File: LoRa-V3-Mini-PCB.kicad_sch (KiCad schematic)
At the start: 23 parts, among them Q1 NA, SW1 Application Button, SW2 MCU Reset, U1 Lora-E5, U2 BR24G1MFVT, U3 SHT40, U4 TSL25911

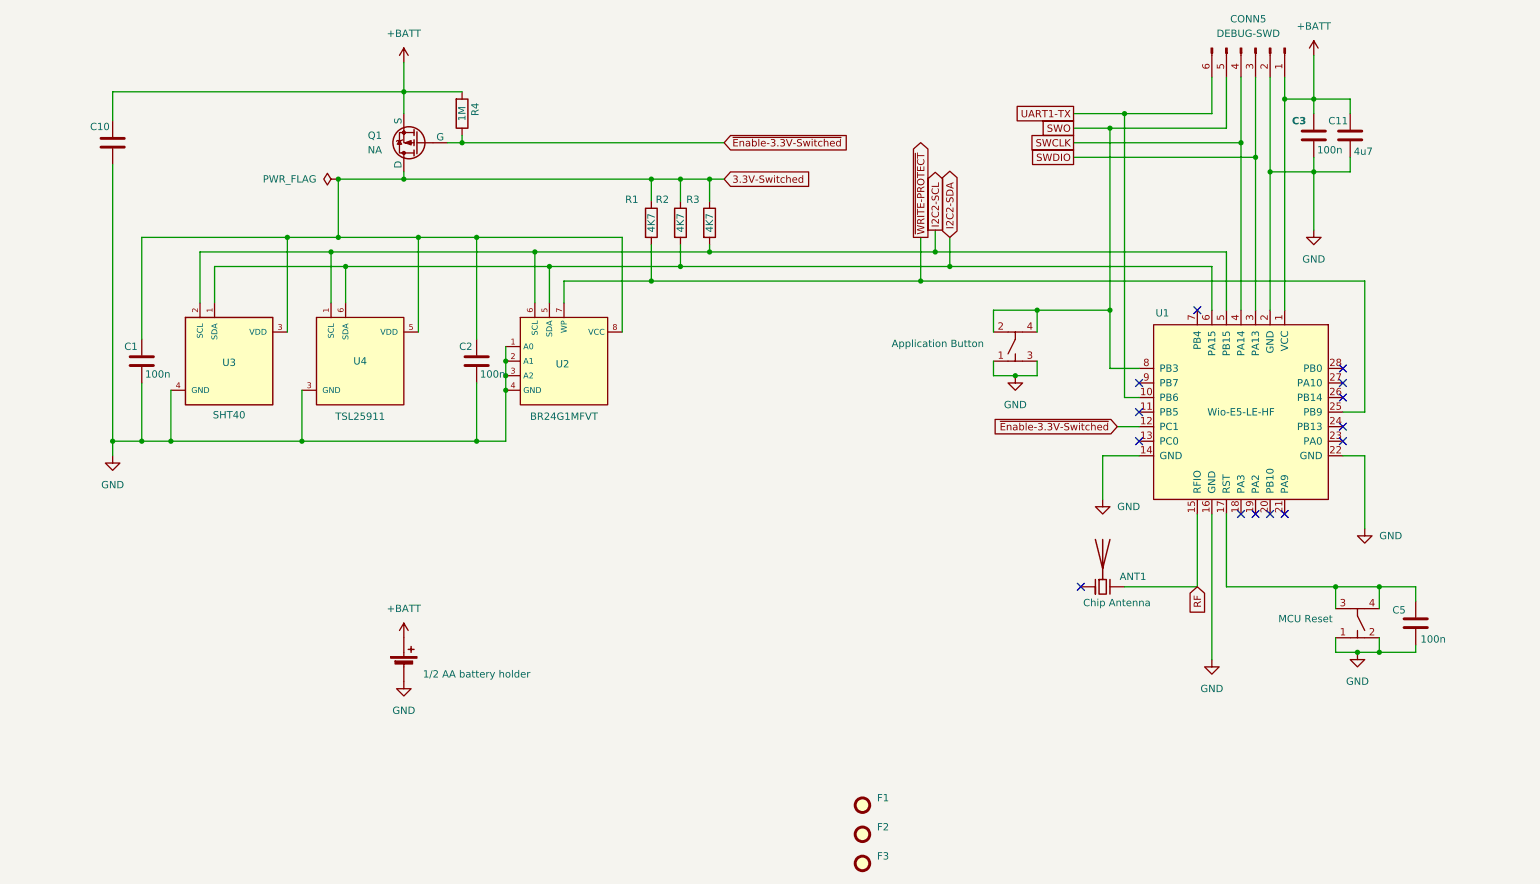
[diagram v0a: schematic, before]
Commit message: try fix error on GND needing datasheet...
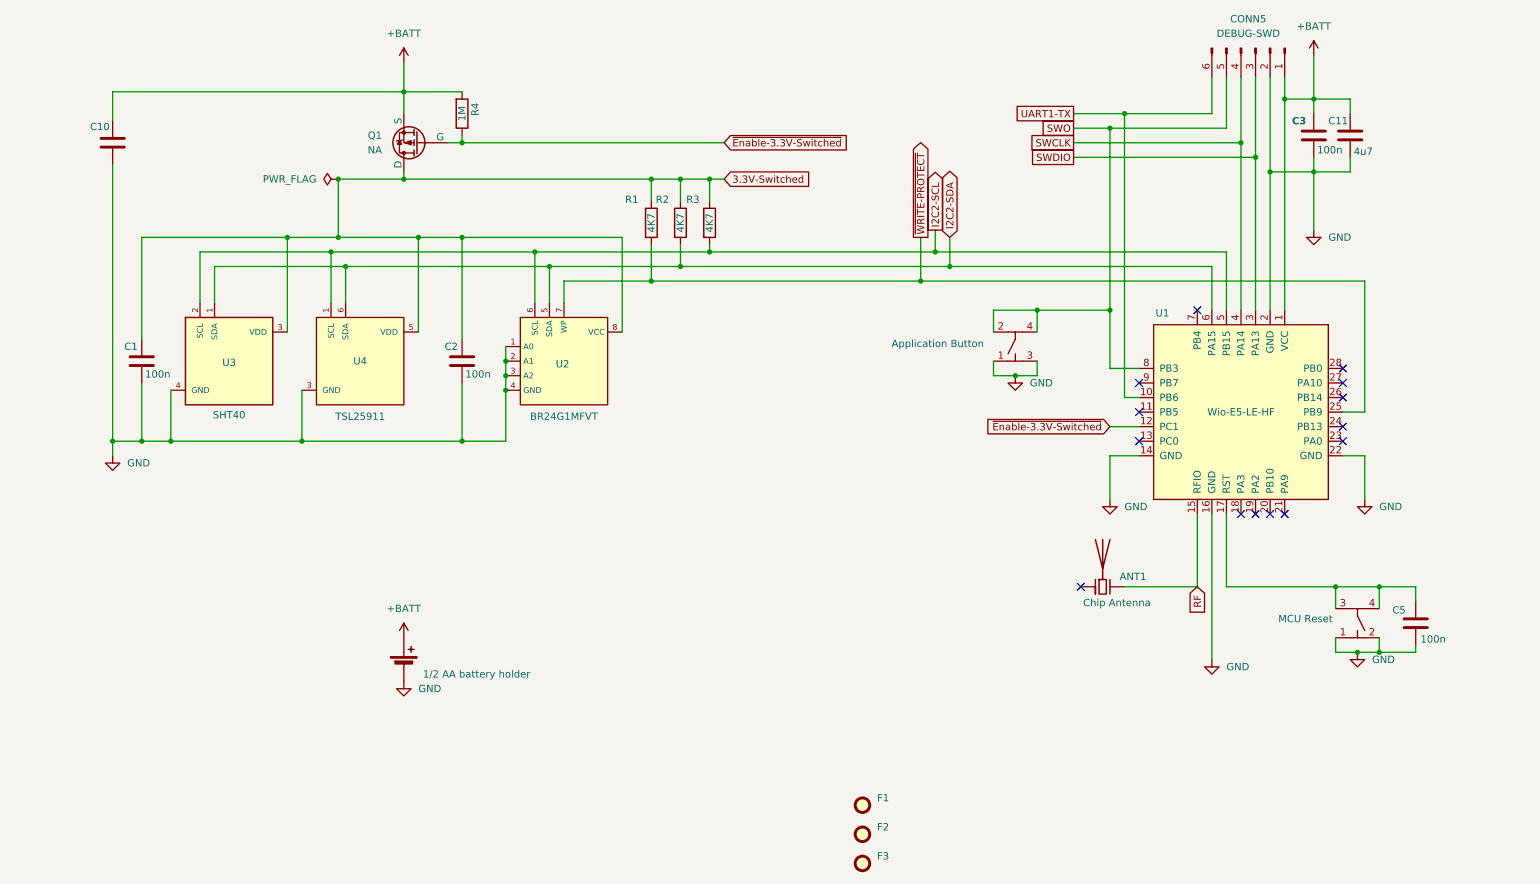
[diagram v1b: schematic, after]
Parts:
- F1, F2, F3: now left out of the parts list
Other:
- moved on the sheet: C2

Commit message: rename GPN to genericPartNumber
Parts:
- ANT1, BH1, C10, C11, CONN5, F1, F2, F3, Q1, SW1, SW2, U1, U2, U3, U4: GPN NA -> (none); genericPartNumber (none) -> NA
- C1, C2, C3, C5: GPN GPC0603104-25-X7R -> (none); genericPartNumber (none) -> GPC0603104-25-X7R
- R1, R2, R3: GPN 4K7 -> (none); genericPartNumber (none) -> 4K7
- R4: GPN 330K -> (none); genericPartNumber (none) -> 330K

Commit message: exclude conn5 from BOM
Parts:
- CONN5: now left out of the parts list
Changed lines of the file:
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@@
 		(unit 1)
 		(exclude_from_sim no)
-		(in_bom yes)
+		(in_bom no)
 		(on_board yes)
 		(dnp no)

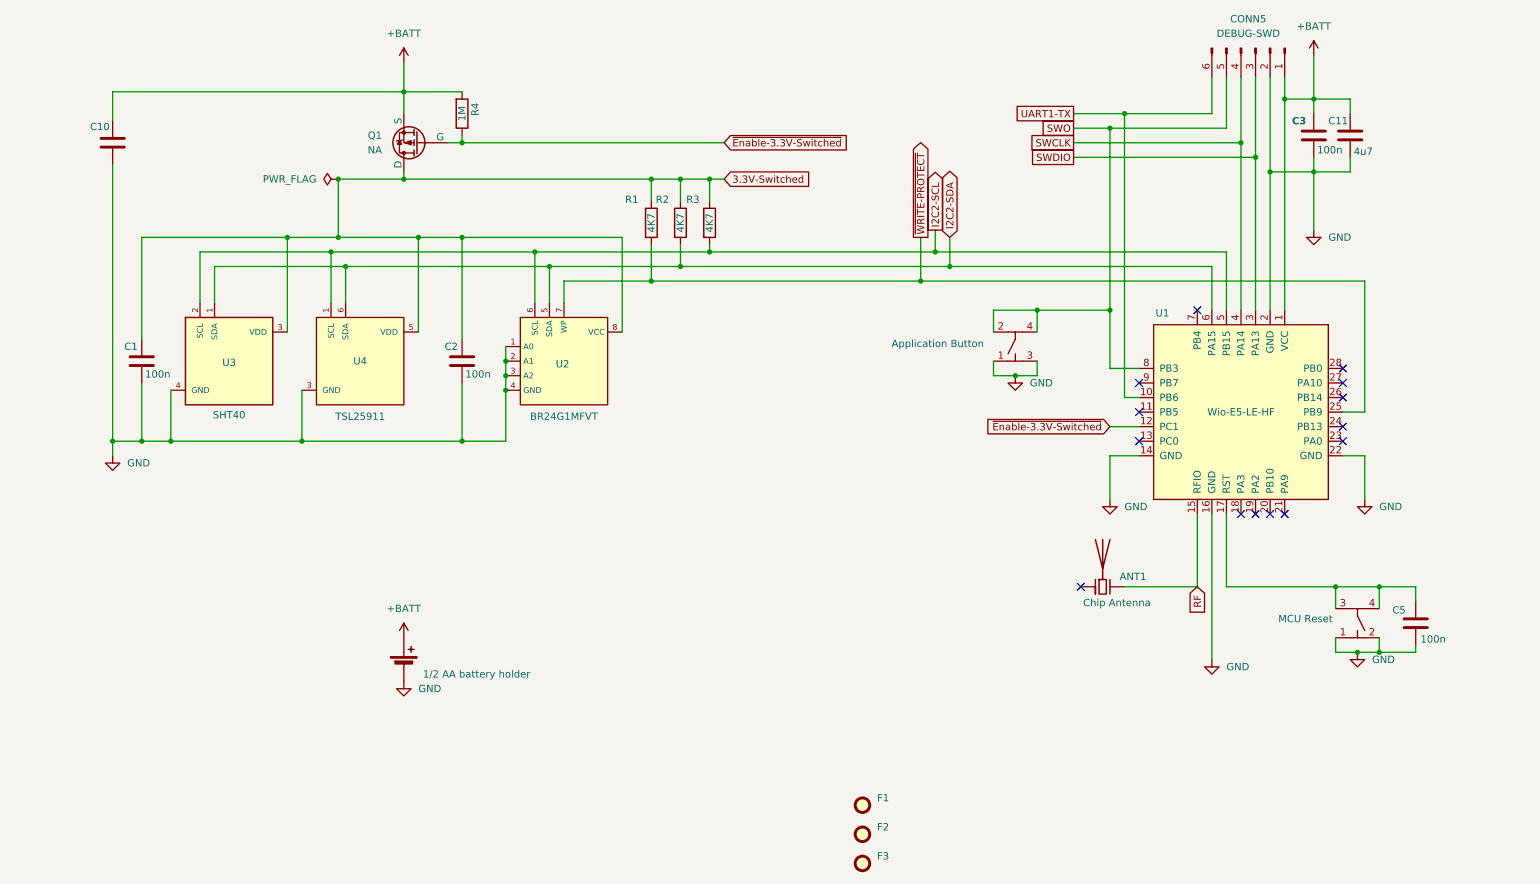
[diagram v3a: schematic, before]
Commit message: Add Pads for CLI connector
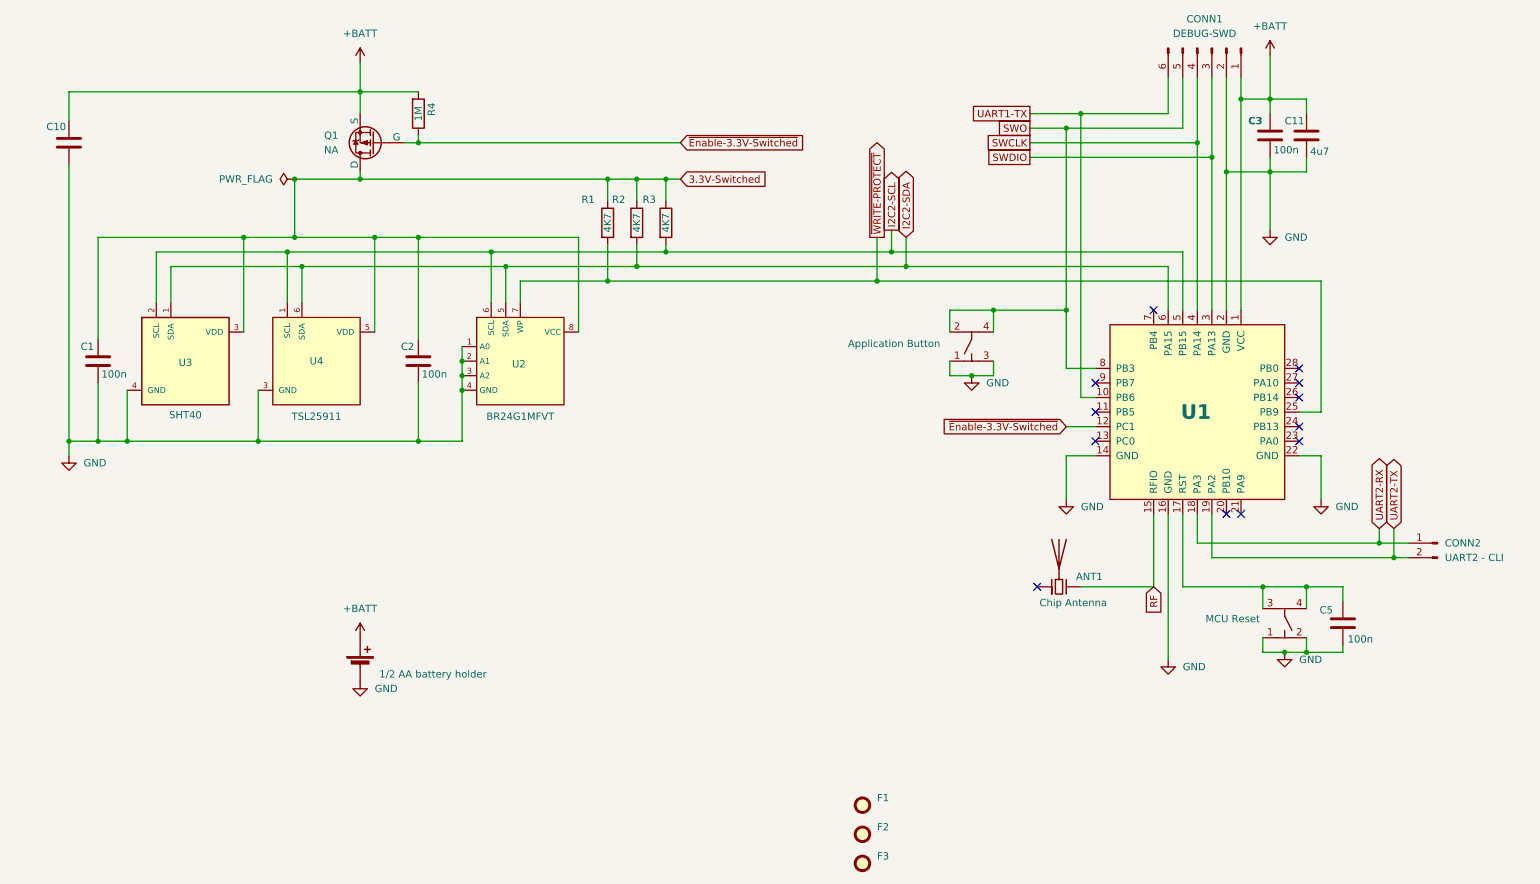
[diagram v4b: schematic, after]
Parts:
- added CONN2: UART2 - CLI, 1projectLibrary:CliConnector_2p, symbol 1projectLibrary:CliConnector-2p
- renumbered CONN5 to CONN1
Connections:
- net UART2-RX: now reaches U1.18 (PA3)
- net UART2-RX: now also CONN2.1 (Pin_1)
- net UART2-TX: now reaches U1.19 (PA2)
- net UART2-TX: now also CONN2.2 (Pin_2)
- no-connect marks 14 -> 12
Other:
- moved on the sheet: ANT1, C1, C10, C11, C2, C3, C5, CONN1, Q1, R1, R2, R3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

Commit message: fix BOM
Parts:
- U1: value Lora-E5 -> Seeed_Wio-E5 LE
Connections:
- net TEST0: now reaches U1.28 (PB0)
- no-connect marks 12 -> 11
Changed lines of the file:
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@@
 	)
 	(no_connect
-		(at 243.84 99.06)
-	)
-	(no_connect
 		(at 231.14 124.46)
 	)
@@
 	(wire
 		(pts
+			(xy 243.84 99.06) (xy 251.46 99.06)
+		)
+		(stroke
+			(width 0)
+			(type default)
+		)
+	)
+	(wire
+		(pts
 			(xy 208.28 104.14) (xy 205.74 104.14)
 		)
@@
 		)
 	)
+	(global_label "TEST0"
+		(shape output)
+		(at 251.46 99.06 0)
+		(fields_autoplaced yes)
+		(effects
+			(font
+				(size 1.27 1.27)
+			)
+			(justify left)
+		)
+		(property "Intersheetrefs" "${INTERSHEET_REFS}"
+			(at 259.9484 99.06 0)
+			(effects
+				(font
+					(size 1.27 1.27)
+				)
+				(justify left)
+				(hide yes)
+			)
+		)
+	)
 	(global_label "RF"
 		(shape input)
@@
 			)
 		)
-		(property "Value" "Lora-E5"
+		(property "Value" "Seeed_Wio-E5 LE"
 			(at 226.187 106.807 90)
 			(effects

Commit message: update bom
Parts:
- SW1: manufacturerName Wurth Elektronik -> Wurth Electronics; manufacturerPartNumber 434351045816 -> 434331045822; octopartUrl https://octopart.com/434351045816-wurth+elektronik-22866030 -> https://octopart.com/434331045822-wurth+elektronik-22866031
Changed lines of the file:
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@@
 			)
 		)
-		(property "Datasheet" "https://octopart.com/datasheet/434351045816-wurth+elektronik-22866030"
+		(property "Datasheet" "https://www.we-online.com/katalog/datasheet/434331045822.pdf"
 			(at 185.674 89.662 0)
 			(effects
@@
 			)
 		)
-		(property "manufacturerName" "Wurth Elektronik"
+		(property "manufacturerName" "Wurth Electronics"
 			(at 186.69 85.09 0)
 			(effects
@@
 			)
 		)
-		(property "manufacturerPartNumber" "434351045816"
+		(property "manufacturerPartNumber" "434331045822"
 			(at 186.69 87.63 0)
 			(effects
@@
 			)
 		)
-		(property "octopartUrl" "https://octopart.com/434351045816-wurth+elektronik-22866030"
+		(property "octopartUrl" "https://octopart.com/434331045822-wurth+elektronik-22866031"
 			(at 186.69 95.25 0)
 			(effects

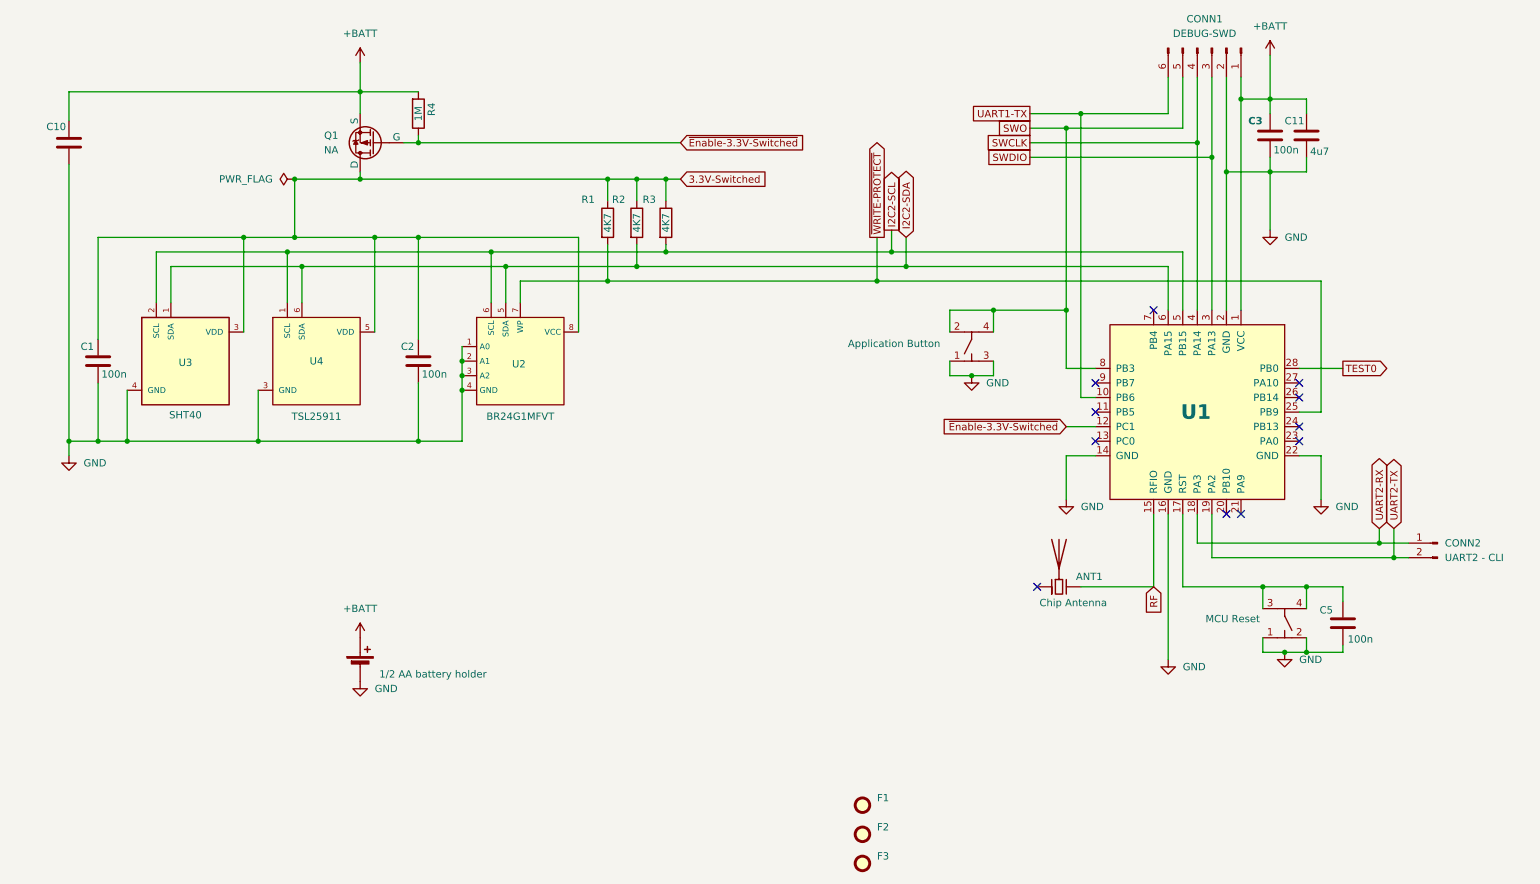
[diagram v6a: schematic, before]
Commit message: add VBUS to detect CLI
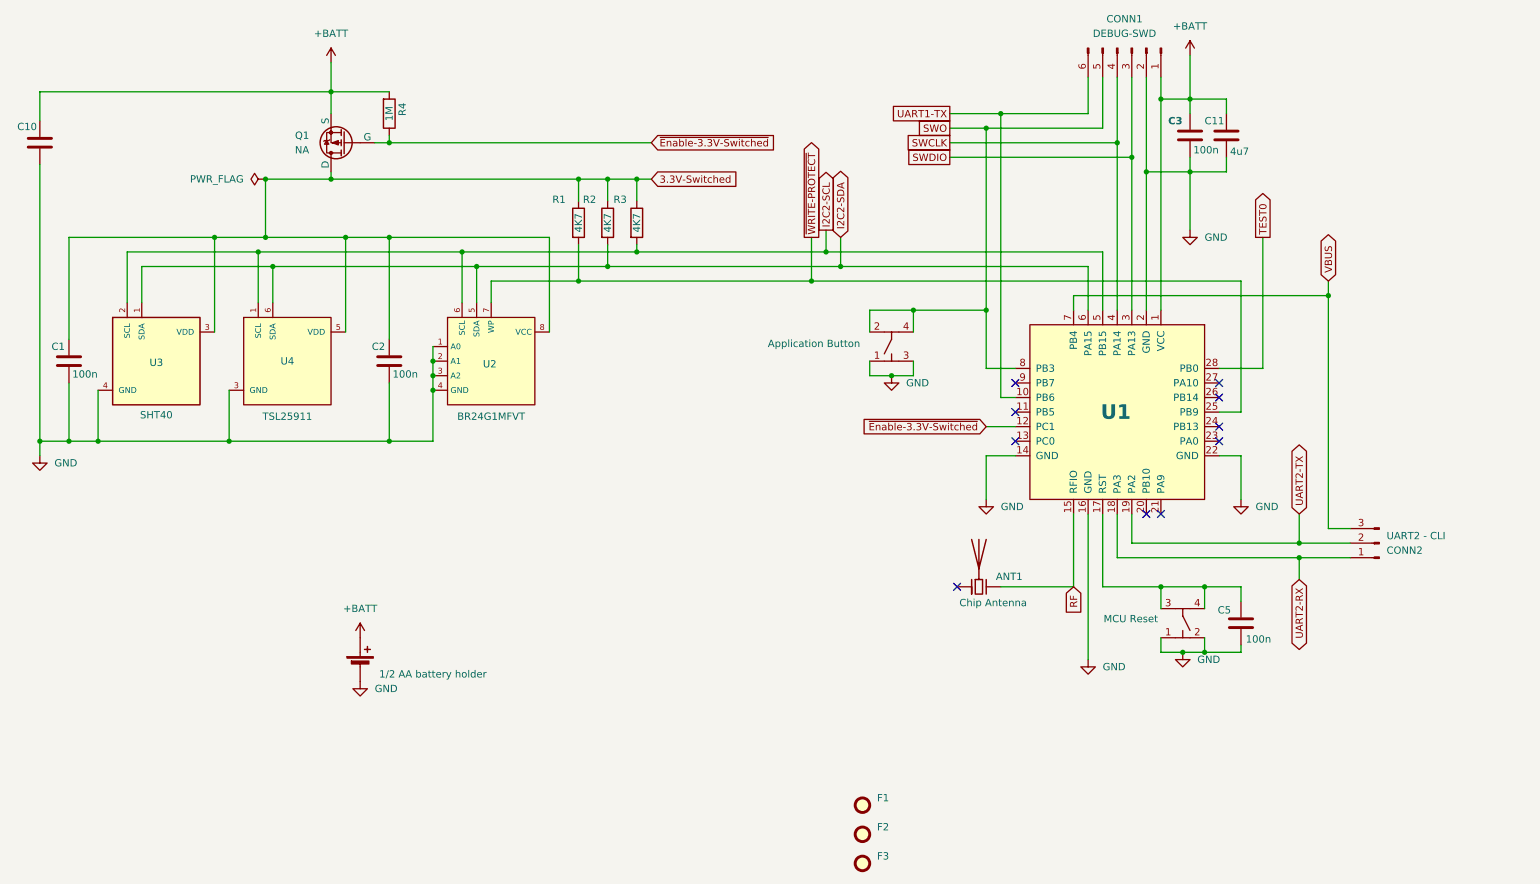
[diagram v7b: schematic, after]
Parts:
- CONN2: footprint 1projectLibrary:CliConnector_2p -> 1projectLibrary:CliConnector_3p; symbol 1projectLibrary:CliConnector-2p -> 1projectLibrary:CLI_Conn_01x03_Pin
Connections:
- net VBUS: now reaches U1.7 (PB4)
- net VBUS: now also CONN2.3 (Pin_3)
- no-connect marks 11 -> 10
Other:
- moved on the sheet: ANT1, C1, C10, C11, C2, C3, C5, CONN1, Q1, R1, R2, R3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
